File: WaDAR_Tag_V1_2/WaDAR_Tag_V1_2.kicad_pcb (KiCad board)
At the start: 2 copper layers, 34.8 x 41.9 mm, 10 parts, among them J1 SMA-J-P-H-RA-TH1, U1 SIT1534AI-H4-DCC-00.001E

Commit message: PCB
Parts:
- removed TP1: VCC, JLab_FP:EpicTestPointV1
- removed TP5: GND, JLab_FP:EpicTestPointV1
- U1: value SIT1534AI-H4-DCC-00.001E -> SiT1569; footprint WADARfootprints:XTAL4_SiT1533_SIT -> Library:SiT1569
- moved J1 13.7 mm to (163.6, 81.3), turned to 180 degrees
- moved C2 11.5 mm to (151.3, 69.4), turned to 90 degrees
- moved C4 9.95 mm to (152.5, 69.4)
- moved C1 6.27 mm to (150.1, 69.4)
- moved U2 5.45 mm to (154.6, 74.5)
- moved C3 5.35 mm to (163.6, 72.5)
- moved U1 2.75 mm to (156.9, 74.0)
- moved BT1 0.39 mm to (163.6, 57.0)
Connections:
- U1 pad 2: GND -> Net-(U1-CLK_Out)
- U1 pad 3: Net-(U1-CLK_Out) -> Net-(BT1-+)
- U1 pad 4: Net-(BT1-+) -> GND
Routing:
- net Net-(U2-OUTPUT1): track 3.30 -> 9.67 mm
- net Net-(U2-INPUT): track 2.92 -> 9.24 mm
- net Net-(BT1-+): track 40.7 -> 46.2 mm
- net Net-(U1-CLK_Out): track 5.53 -> 10.6 mm
- net Net-(C3-Pad2): track 12.8 -> 7.86 mm
- net GND: track 7.26 -> 4.00 mm, vias 1 -> 14
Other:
- board size 34.8 x 41.9 mm -> 35 x 40 mm
- board text added: "RF-Backscatter-V1.2 J-Lab UCSC"
- board text removed: "GND"
- board text removed: "J1"
- board text removed: "RF-Backscatter-V1.1 J-Lab UCSC"
- board text removed: "VCC"

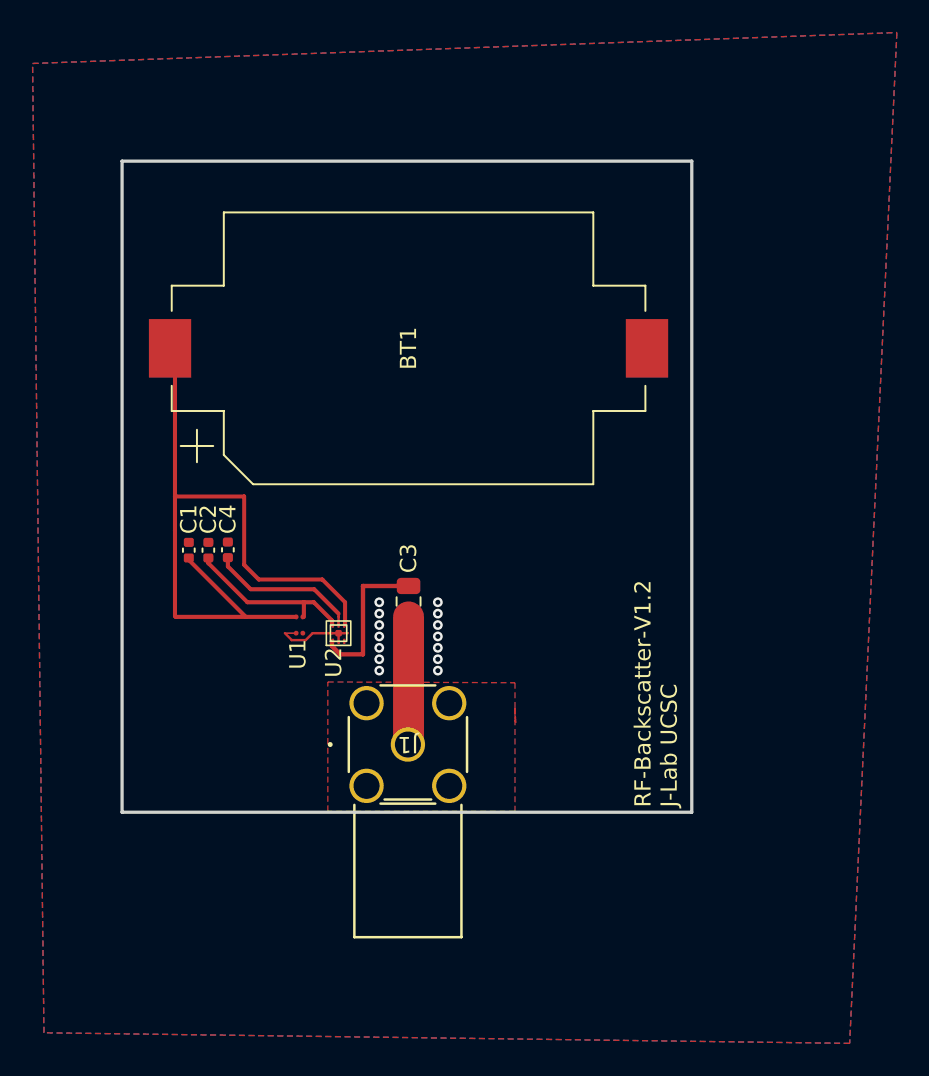
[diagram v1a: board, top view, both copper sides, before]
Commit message: added test points, made PCB double sided
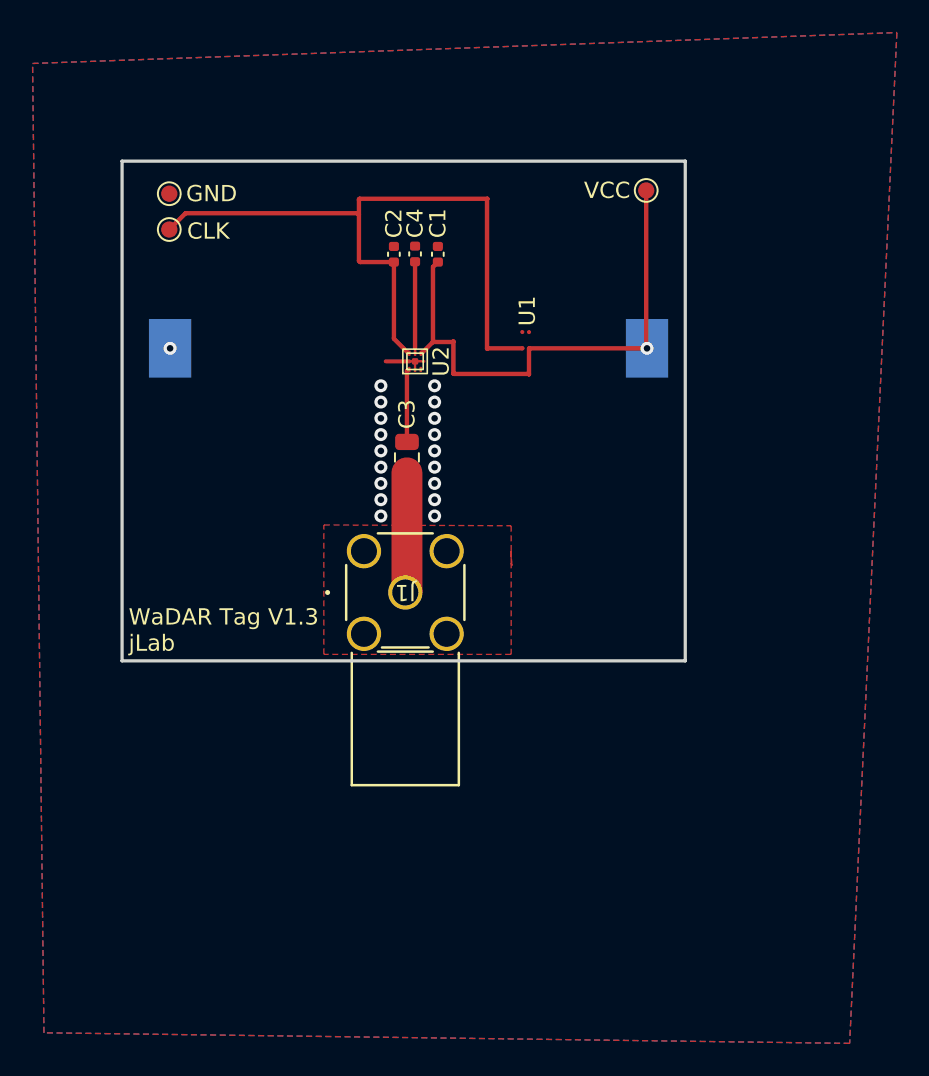
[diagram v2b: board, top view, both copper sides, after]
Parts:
- added CLK: CLK, TestPoint:TestPoint_Pad_D1.0mm, F.Cu at (148.9, 49.7)
- added GND: GND, TestPoint:TestPoint_Pad_D1.0mm, F.Cu at (148.9, 47.5)
- added VCC: VCC, TestPoint:TestPoint_Pad_D1.0mm, F.Cu at (178.2, 47.3)
- BT1: moved to B.Cu
- moved C1 23.8 mm to (165.4, 51.2)
- moved U1 22.3 mm to (170.8, 56.5), turned to -90 degrees
- moved C4 21.5 mm to (164.0, 51.2)
- moved C2 21.5 mm to (162.7, 51.2)
- moved U2 17.3 mm to (159.2, 57.8)
- moved J1 9.34 mm to (163.4, 72.0)
- moved C3 8.85 mm to (163.5, 63.7)
- turned BT1 to 180 degrees
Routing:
- net Net-(U1-CLK_Out): track 10.6 -> 43.3 mm
- net Net-(BT1-+): track 46.2 -> 32.4 mm, vias 0 -> 1
- net Net-(U2-OUTPUT1): track 9.67 -> 4.50 mm
- net Net-(U2-INPUT): track 9.24 -> 5.62 mm
- net GND: track 4.00 -> 1.45 mm, vias 14 -> 19
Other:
- board size 35 x 40 mm -> 34.6 x 30.7 mm
- board text added: "WaDAR Tag V1.3 jLab"
- board text removed: "RF-Backscatter-V1.2 J-Lab UCSC"

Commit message: updated datasheets
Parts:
- removed CLK: CLK, TestPoint:TestPoint_Pad_D1.0mm
- removed GND: GND, TestPoint:TestPoint_Pad_D1.0mm
- removed VCC: VCC, TestPoint:TestPoint_Pad_D1.0mm
- added TP1: VCC, TestPoint:TestPoint_Pad_D1.0mm, F.Cu at (178.2, 47.3)
- added TP2: GND, TestPoint:TestPoint_Pad_D1.0mm, F.Cu at (148.8, 47.4)
- added TP3: CLK, TestPoint:TestPoint_Pad_D1.0mm, F.Cu at (148.9, 49.8)
- U2: footprint JLab_FP:SKY13351_FP -> Library:SKY13351_FP
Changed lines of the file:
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@@
 	(footprint "TestPoint:TestPoint_Pad_D1.0mm"
 		(layer "F.Cu")
-		(at 148.9 47.5)
+		(at 148.8 47.4)
 		(descr "SMD pad as test Point, diameter 1.0mm")
 		(tags "test point SMD pad")
-		(property "Reference" "GND"
-			(at 2.6 0 0)
+		(property "Reference" "TP2"
+			(at 0 -1.448 0)
 			(layer "F.SilkS")
 			(effects
@@
 			(layers "F.Cu" "F.Mask")
 			(net 1 "GND")
-			(pinfunction "1")
-			(pintype "passive")
-		)
-	)
-	(footprint "TestPoint:TestPoint_Pad_D1.0mm"
-		(layer "F.Cu")
-		(at 148.9 49.7)
-		(descr "SMD pad as test Point, diameter 1.0mm")
-		(tags "test point SMD pad")
-		(property "Reference" "CLK"
-			(at 2.4 0.1 0)
-			(layer "F.SilkS")
-			(effects
-				(font
-					(size 1 1)
-					(thickness 0.15)
-				)
-			)
-		)
-		(property "Value" "CLK"
-			(at 0 1.55 0)
-			(layer "F.Fab")
-			(effects
-				(font
-					(size 1 1)
-					(thickness 0.15)
-				)
-			)
-		)
-		(property "Footprint" "TestPoint:TestPoint_Pad_D1.0mm"
-			(at 0 0 0)
-			(layer "F.Fab")
-			(hide yes)
-			(effects
-				(font
-					(size 1.27 1.27)
-					(thickness 0.15)
-				)
-			)
-		)
-		(property "Datasheet" ""
-			(at 0 0 0)
-			(layer "F.Fab")
-			(hide yes)
-			(effects
-				(font
-					(size 1.27 1.27)
-					(thickness 0.15)
-				)
-			)
-		)
-		(property "Description" "test point"
-			(at 0 0 0)
-			(layer "F.Fab")
-			(hide yes)
-			(effects
-				(font
-					(size 1.27 1.27)
-					(thickness 0.15)
-				)
-			)
-		)
-		(property ki_fp_filters "Pin* Test*")
-		(sheetname "Root")
-		(sheetfile "WaDAR_Tag_V1_2.kicad_sch")
-		(attr exclude_from_pos_files)
-		(fp_circle
-			(center 0 0)
-			(end 0 0.7)
-			(stroke
-				(width 0.12)
-				(type solid)
-			)
-			(fill none)
-			(layer "F.SilkS")
-		)
-		(fp_circle
-			(center 0 0)
-			(end 1 0)
-			(stroke
-				(width 0.05)
-				(type solid)
-			)
-			(fill none)
-			(layer "F.CrtYd")
-		)
-		(fp_text user "${REFERENCE}"
-			(at 0 -1.45 0)
-			(layer "F.Fab")
-			(effects
-				(font
-					(size 1 1)
-					(thickness 0.15)
-				)
-			)
-		)
-		(pad "1" smd circle
-			(at 0 0)
-			(size 1 1)
-			(layers "F.Cu" "F.Mask")
-			(net 3 "Net-(U1-CLK_Out)")
 			(pinfunction "1")
 			(pintype "passive")
@@
 		(descr "SMD pad as test Point, diameter 1.0mm")
 		(tags "test point SMD pad")
-		(property "Reference" "VCC"
-			(at -2.4 0 0)
+		(property "Reference" "TP1"
+			(at 0 -1.448 0)
 			(layer "F.SilkS")
 			(effects
@@
 		)
 	)
-	(footprint "JLab_FP:SKY13351_FP"
+	(footprint "TestPoint:TestPoint_Pad_D1.0mm"
+		(layer "F.Cu")
+		(at 148.9 49.8)
+		(descr "SMD pad as test Point, diameter 1.0mm")
+		(tags "test point SMD pad")
+		(property "Reference" "TP3"
+			(at 0 -1.448 0)
+			(layer "F.SilkS")
+			(effects
+				(font
+					(size 1 1)
+					(thickness 0.15)
+				)
+			)
+		)
+		(property "Value" "CLK"
+			(at 0 1.55 0)
+			(layer "F.Fab")
+			(effects
+				(font
+					(size 1 1)
+					(thickness 0.15)
+				)
+			)
+		)
+		(property "Footprint" "TestPoint:TestPoint_Pad_D1.0mm"
+			(at 0 0 0)
+			(layer "F.Fab")
+			(hide yes)
+			(effects
+				(font
+					(size 1.27 1.27)
+					(thickness 0.15)
+				)
+			)
+		)
+		(property "Datasheet" ""
+			(at 0 0 0)
+			(layer "F.Fab")
+			(hide yes)
+			(effects
+				(font
+					(size 1.27 1.27)
+					(thickness 0.15)
+				)
+			)
+		)
+		(property "Description" "test point"
+			(at 0 0 0)
+			(layer "F.Fab")
+			(hide yes)
+			(effects
+				(font
+					(size 1.27 1.27)
+					(thickness 0.15)
+				)
+			)
+		)
+		(property ki_fp_filters "Pin* Test*")
+		(sheetname "Root")
+		(sheetfile "WaDAR_Tag_V1_2.kicad_sch")
+		(attr exclude_from_pos_files)
+		(fp_circle
+			(center 0 0)
+			(end 0 0.7)
+			(stroke
+				(width 0.12)
+				(type solid)
+			)
+			(fill none)
+			(layer "F.SilkS")
+		)
+		(fp_circle
+			(center 0 0)
+			(end 1 0)
+			(stroke
+				(width 0.05)
+				(type solid)
+			)
+			(fill none)
+			(layer "F.CrtYd")
+		)
+		(fp_text user "${REFERENCE}"
+			(at 0 -1.45 0)
+			(layer "F.Fab")
+			(effects
+				(font
+					(size 1 1)
+					(thickness 0.15)
+				)
+			)
+		)
+		(pad "1" smd circle
+			(at 0 0)
+			(size 1 1)
+			(layers "F.Cu" "F.Mask")
+			(net 3 "Net-(U1-CLK_Out)")
+			(pinfunction "1")
+			(pintype "passive")
+		)
+	)
+	(footprint "Library:SKY13351_FP"
 		(layer "F.Cu")
 		(at 159.25 57.8 90)
 		(property "Reference" "U2"
-			(at 0 6.35 90)
+			(at 0 -0.5 90)
 			(unlocked yes)
 			(layer "F.SilkS")
@@
 				(font
 					(size 1 1)
-					(thickness 0.15)
+					(thickness 0.1)
 				)
 			)
@@
 			(unlocked yes)
 			(layer "F.Fab")
-			(hide yes)
-			(effects
-				(font
-					(size 1 1)
-					(thickness 0.15)
-				)
-			)
-		)
-		(property "Footprint" "JLab_FP:SKY13351_FP"
+			(effects
+				(font
+					(size 1 1)
+					(thickness 0.15)
+				)
+			)
+		)
+		(property "Footprint" "Library:SKY13351_FP"
 			(at 0 0 90)
 			(layer "F.Fab")

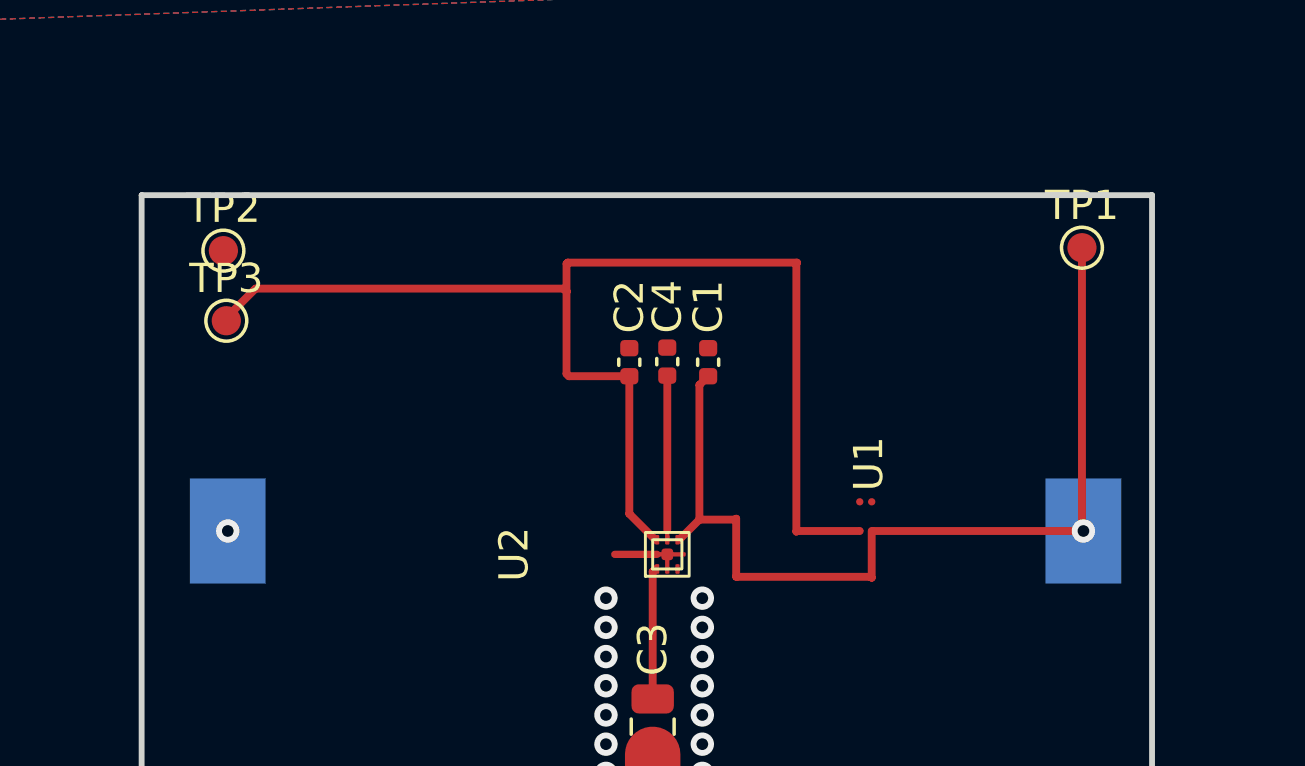
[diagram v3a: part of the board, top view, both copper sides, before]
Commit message: fixed all absolute pathing issues
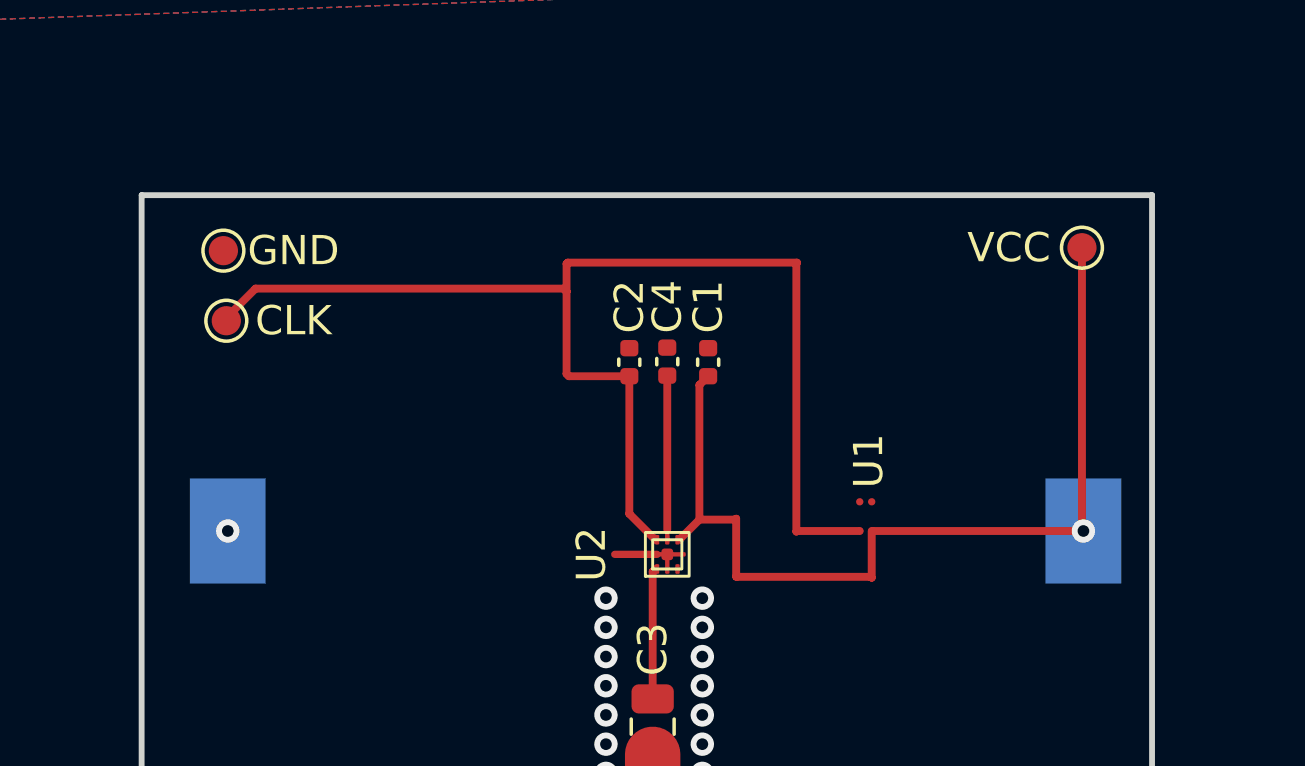
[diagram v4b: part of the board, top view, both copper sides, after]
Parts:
- BT1: value Battery_Cell -> 1060
- U1: value SiT1569 -> SIT1569AC-J3-30E-0000.080000
- U2: value ~ -> SKY13351-378LF
- renumbered TP3 to CLK, TP2 to GND, TP1 to VCC
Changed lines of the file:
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@@
 			)
 		)
-		(property "Datasheet" ""
+		(property "Datasheet" "https://mm.digikey.com/Volume0/opasdata/d220001/medias/docus/2969/CL05C330JB5NNNC_Spec.pdf"
 			(at 0 0 90)
 			(unlocked yes)
@@
 			)
 		)
-		(property "Description" "0402CG330J500NT"
+		(property "Description" "CAP CER 33PF 50V C0G/NP0 0402"
 			(at 0 0 90)
 			(unlocked yes)
@@
 			)
 		)
+		(property ki_fp_filters "C_*")
 		(sheetname "Root")
 		(sheetfile "WaDAR_Tag_V1_2.kicad_sch")
@@
 		(descr "SMD pad as test Point, diameter 1.0mm")
 		(tags "test point SMD pad")
-		(property "Reference" "TP2"
-			(at 0 -1.448 0)
+		(property "Reference" "GND"
+			(at 2.4 0 0)
 			(layer "F.SilkS")
 			(effects
@@
 			)
 		)
-		(property "Datasheet" ""
+		(property "Datasheet" "https://mm.digikey.com/Volume0/opasdata/d220001/medias/docus/2969/CL05C330JB5NNNC_Spec.pdf"
 			(at 0 0 90)
 			(unlocked yes)
@@
 			)
 		)
-		(property "Description" "0402CG330J500NT"
+		(property "Description" "CAP CER 33PF 50V C0G/NP0 0402"
 			(at 0 0 90)
 			(unlocked yes)
@@
 			)
 		)
+		(property ki_fp_filters "C_*")
 		(sheetname "Root")
 		(sheetfile "WaDAR_Tag_V1_2.kicad_sch")
@@
 		(descr "SMD pad as test Point, diameter 1.0mm")
 		(tags "test point SMD pad")
-		(property "Reference" "TP1"
-			(at 0 -1.448 0)
+		(property "Reference" "VCC"
+			(at -2.5 0 0)
 			(layer "F.SilkS")
 			(effects
@@
 			)
 		)
-		(property "Datasheet" "CC0402KRX7R6BB103"
+		(property "Datasheet" "https://search.kemet.com/download/datasheet/C0805C101J5GAC7800"
 			(at 0 0 -90)
 			(unlocked yes)
@@
 			)
 		)
-		(property "Description" ""
+		(property "Description" "CAP CER 100PF 50V C0G/NP0 0805"
 			(at 0 0 -90)
 			(unlocked yes)
@@
 			)
 		)
-		(property ki_fp_filters "CAPC10555_55N_KEM CAPC10555_55N_KEM-M CAPC10555_55N_KEM-L")
+		(property ki_fp_filters "C_*")
 		(sheetname "Root")
 		(sheetfile "WaDAR_Tag_V1_2.kicad_sch")
@@
 			(roundrect_rratio 0.25)
 			(net 8 "Net-(U2-OUTPUT1)")
-			(pintype "unspecified")
+			(pintype "passive")
 		)
 		(pad "2" smd roundrect
@@
 			(roundrect_rratio 0.25)
 			(net 4 "Net-(C3-Pad2)")
-			(pintype "unspecified")
+			(pintype "passive")
 		)
 		(model "${KICAD8_3DMODEL_DIR}/Capacitor_SMD.3dshapes/C_0805_2012Metric.wrl"
@@
 		(descr "SMD pad as test Point, diameter 1.0mm")
 		(tags "test point SMD pad")
-		(property "Reference" "TP3"
-			(at 0 -1.448 0)
+		(property "Reference" "CLK"
+			(at 2.3 0 0)
 			(layer "F.SilkS")
 			(effects
@@
 		(at 159.25 57.8 90)
 		(property "Reference" "U2"
-			(at 0 -0.5 90)
+			(at 0 2.15 90)
 			(unlocked yes)
 			(layer "F.SilkS")
@@
 			)
 		)
-		(property "Value" "~"
+		(property "Value" "SKY13351-378LF"
 			(at 0 1 90)
 			(unlocked yes)
@@
 			)
 		)
-		(property "Datasheet" ""
+		(property "Datasheet" "https://www.skyworksinc.com/-/media/5E82DAE396A64F5D8598F71A4EC4B215.pdf"
 			(at 0 0 90)
 			(layer "F.Fab")
@@
 			)
 		)
-		(property "Description" ""
+		(property "Description" "IC RF SWITCH SPDT 6GHZ 6MLPD"
 			(at 0 0 90)
 			(layer "F.Fab")
@@
 		(at 170.795 56.5 -90)
 		(property "Reference" "U1"
-			(at -1.8 -0.1 90)
+			(at -1.9 -0.1 90)
 			(unlocked yes)
 			(layer "F.SilkS")
@@
 			)
 		)
-		(property "Value" "SiT1569"
+		(property "Value" "SIT1569AC-J3-30E-0000.080000"
 			(at -5 -5.63 -90)
 			(unlocked yes)
@@
 			)
 		)
-		(property "Datasheet" ""
+		(property "Datasheet" "https://www.sitime.com/datasheet/SiT1569"
 			(at -5 -6.63 -90)
 			(unlocked yes)
@@
 			)
 		)
-		(property "Description" ""
+		(property "Description" "MEMS OSC XO 80HZ LVCMOS"
 			(at -5 -6.63 -90)
 			(unlocked yes)
@@
 			)
 		)
-		(property "Datasheet" ""
+		(property "Datasheet" "https://www.yageo.com/upload/media/product/productsearch/datasheet/mlcc/UPY-GP_NP0_16V-to-50V_18.pdf"
 			(at 0 0 90)
 			(unlocked yes)
@@
 			)
 		)
-		(property "Description" "0402CG330J500NT"
+		(property "Description" "CAP CER 100PF 50V C0G/NPO 0402"
 			(at 0 0 90)
 			(unlocked yes)
@@
 			)
 		)
+		(property ki_fp_filters "C_*")
 		(sheetname "Root")
 		(sheetfile "WaDAR_Tag_V1_2.kicad_sch")
@@
 			)
 		)
-		(property "Value" "Battery_Cell"
+		(property "Value" "1060"
 			(at 5 4.2 0)
 			(layer "B.Fab")
@@
 			)
 		)
-		(property "Datasheet" ""
+		(property "Datasheet" "https://www.keyelco.com/userAssets/file/M65p4.pdf"
 			(at 0 0 0)
 			(unlocked yes)
@@
 			)
 		)
-		(property "Description" "Single-cell battery"
+		(property "Description" "BATTERY HOLDER COIN 20MM SMD"
 			(at 0 0 0)
 			(unlocked yes)
